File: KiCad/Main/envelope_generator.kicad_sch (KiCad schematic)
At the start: 54 parts, among them J7 Screw_Terminal_01x03, J8 Screw_Terminal_01x03, U5 TL074, U6 TL074, U7 TL074

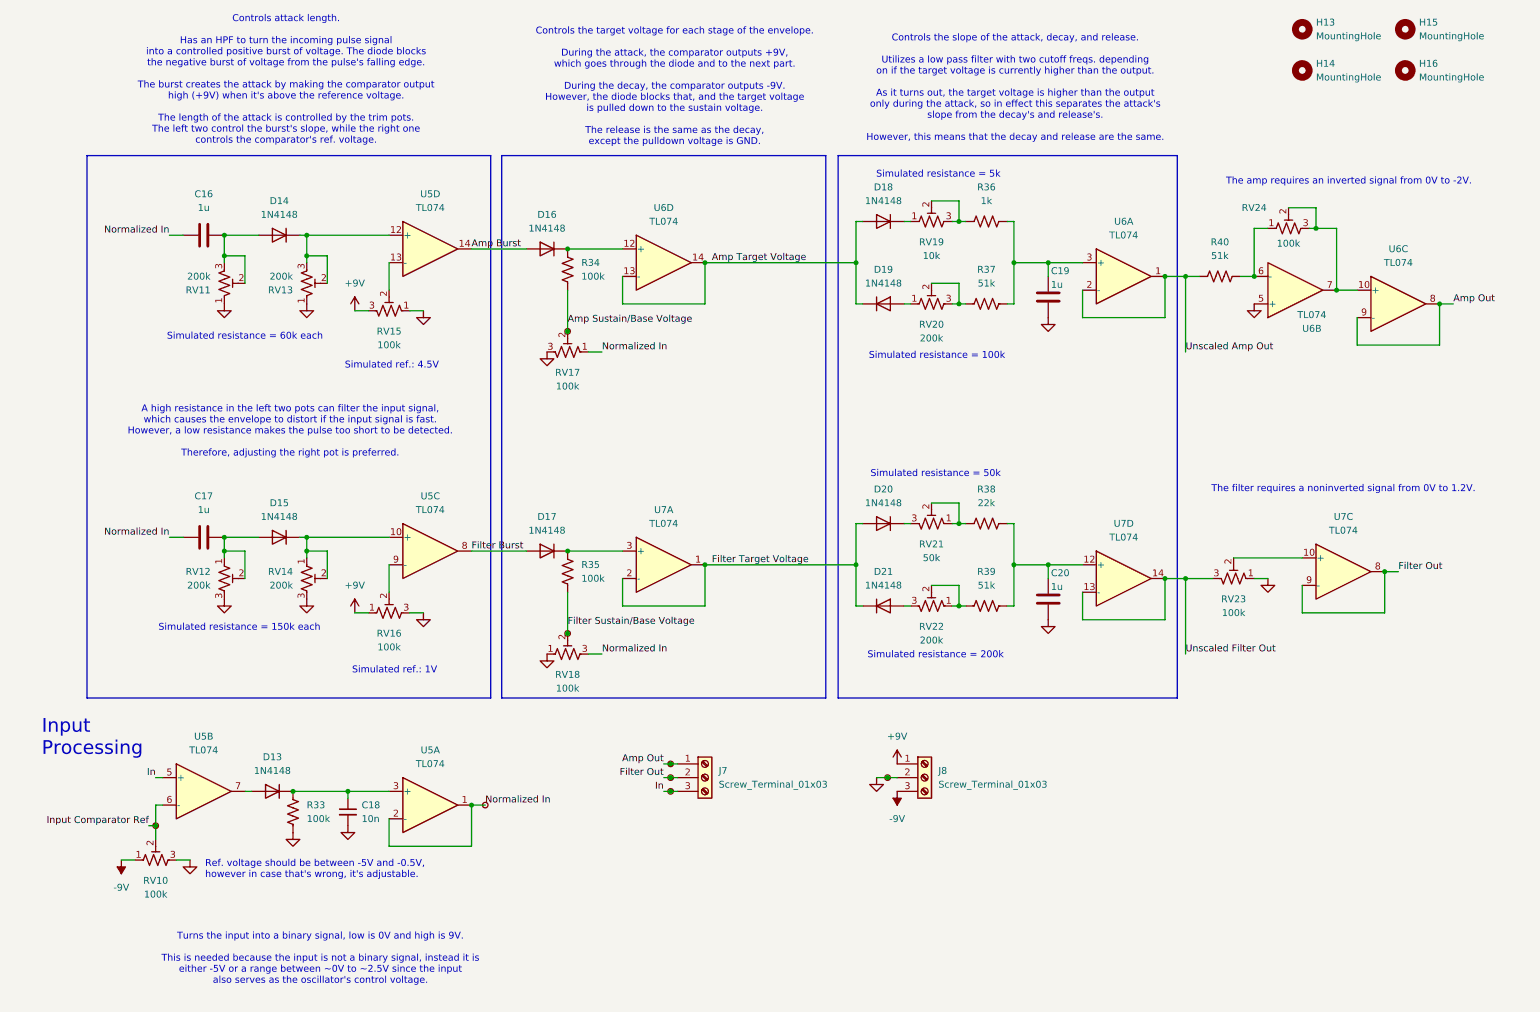
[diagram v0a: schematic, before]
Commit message: merged project into one combined board (excluding the buttons)
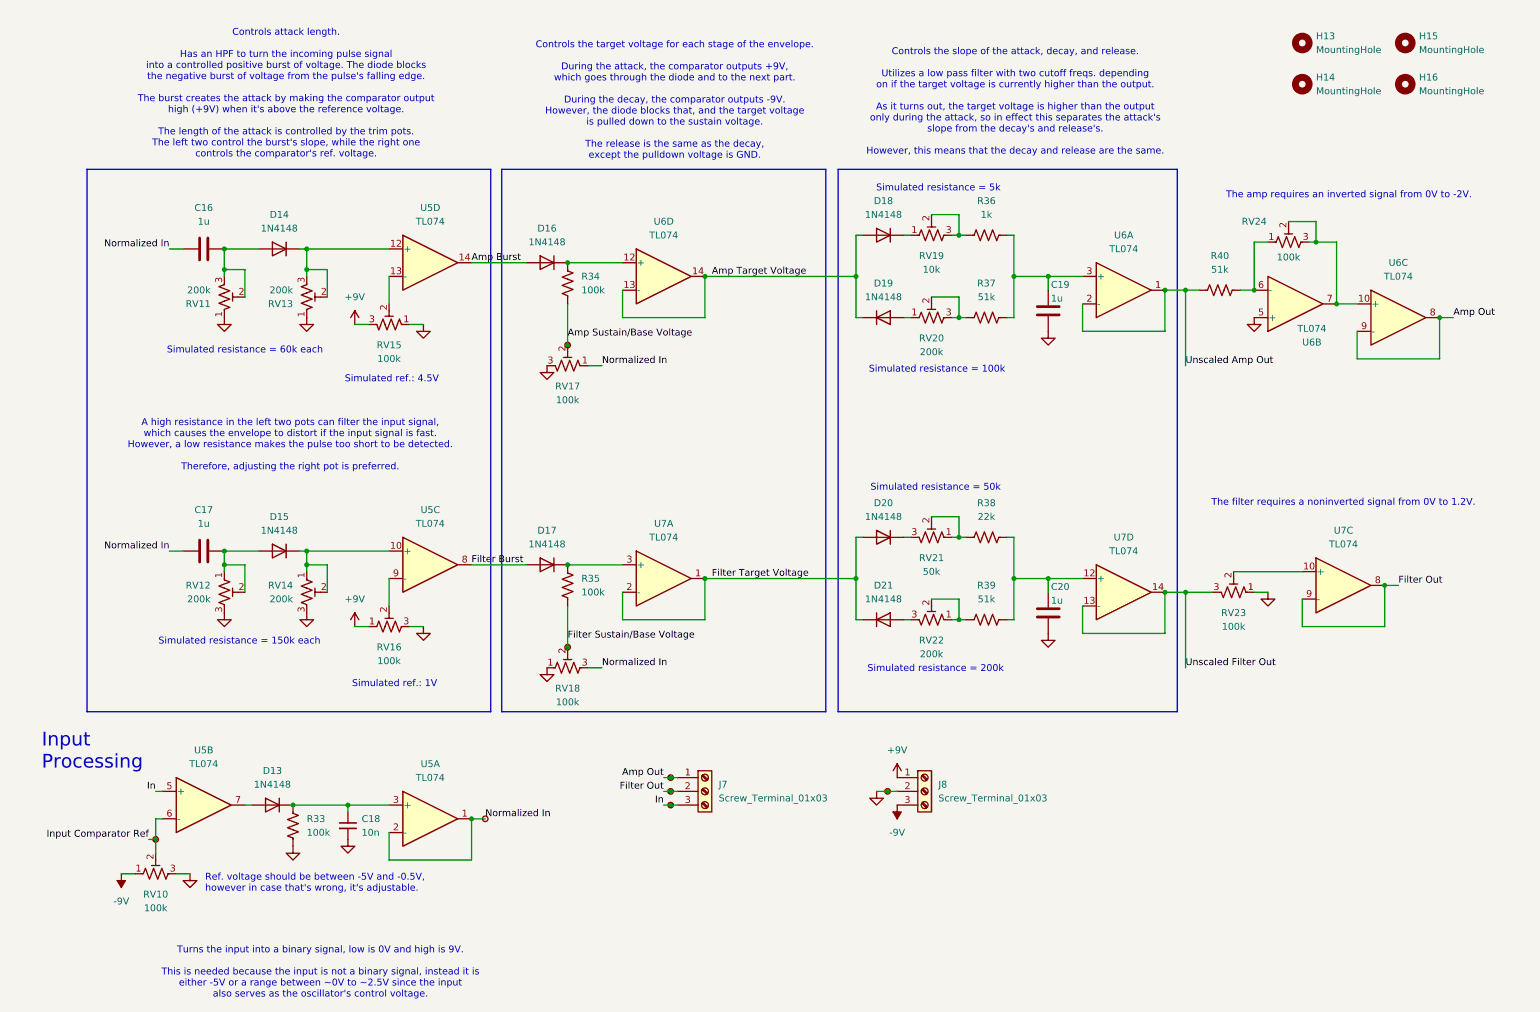
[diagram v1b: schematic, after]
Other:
- moved on the sheet: C16, C17, C18, C19, C20, D13, D14, D15, D16, D17, D18, D19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
